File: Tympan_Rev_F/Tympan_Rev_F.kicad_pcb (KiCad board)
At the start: 4 copper layers, 38 x 74 mm, 93 parts, among them IC1 BC127, J1 SJ-3523-SMT-TR, J2 SJ-3524-SMT-TR-PI, J3 Conn_01x06, J4 Qwiik Connector, J5 Conn_01x24, J6 Conn_01x24, P1 CONN_01X06, P2 CONN_01X06, P3 CONN_01X06, P4 CONN_01X06, P6 CONN_01X01, P7 CONN_01X01, P8 CONN_01X01, SW1 CL-SB-22A, SW2 SW_Push, U1 MCP73831, U2 TLV320AIC3206IRSBT, U3 74LVC1G66, U4 LP5907MFX-1.8, U5 Teensy4.1, U6 LC709203

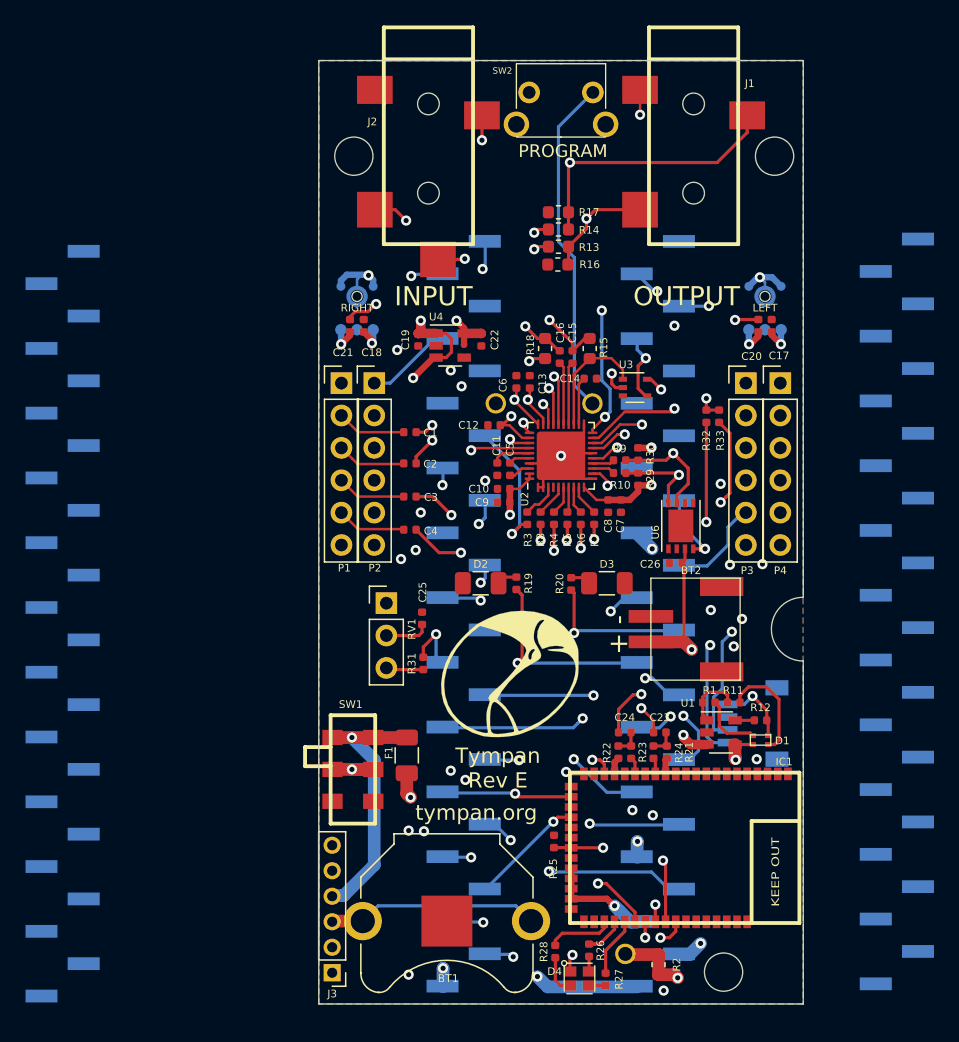
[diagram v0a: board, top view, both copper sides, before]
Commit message: Added SPI
Selected pins to bring SPI connection to the BLE moudule
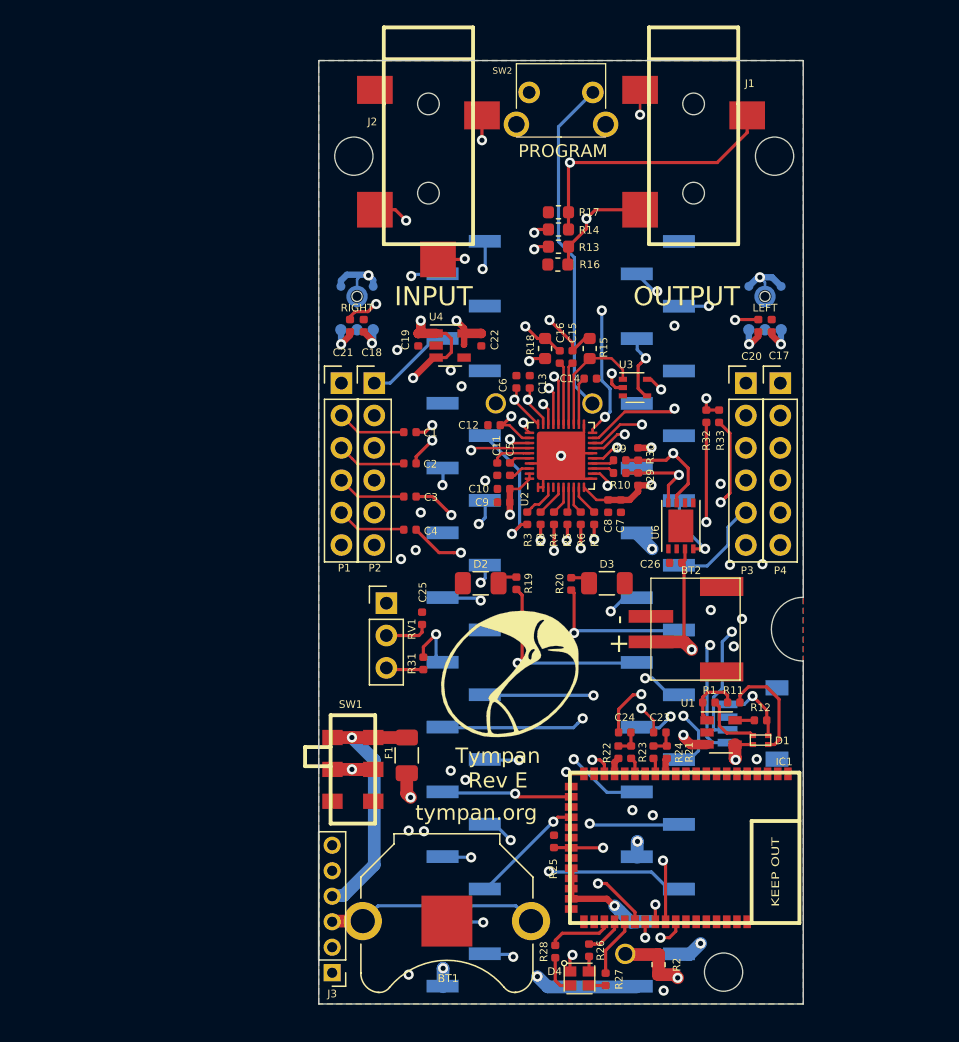
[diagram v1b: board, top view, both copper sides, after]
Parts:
- removed J5, J6: Conn_01x24, Pin_Headers:Pin_Header_Straight_1x24_Pitch2.54mm_SMD_Pin1Left

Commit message: minor edit save
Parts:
- moved J3 0.07 mm to (135.4, 130.7)
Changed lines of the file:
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@@
   )
   (footprint "Pin_Headers:Pin_Header_Straight_1x06_Pitch2.00mm" (layer "F.Cu")
-    (at 135.45 130.75 180)
+    (at 135.4 130.7 180)
     (descr "Through hole straight pin header, 1x06, 2.00mm pitch, single row")
     (tags "Through hole pin header THT 1x06 2.00mm single row")
@@
   (segment (start 142.65 128.1) (end 142.65 119.65) (width 0.25) (layer "In2.Cu") (net 135))
   (segment (start 164.375001 105.051999) (end 164.375001 114.624999) (width 0.25) (layer "In2.Cu") (net 135))
-  (segment (start 135.45 130.75) (end 140 130.75) (width 0.25) (layer "In2.Cu") (net 135))
+  (segment (start 135.4 130.7) (end 139.95 130.7) (width 0.25) (layer "In2.Cu") (net 135))
   (segment (start 162.65 78.47) (end 164.98 78.47) (width 0.25) (layer "B.Cu") (net 135))
   (segment (start 164.98 78.47) (end 165 78.45) (width 0.25) (layer "B.Cu") (net 135))

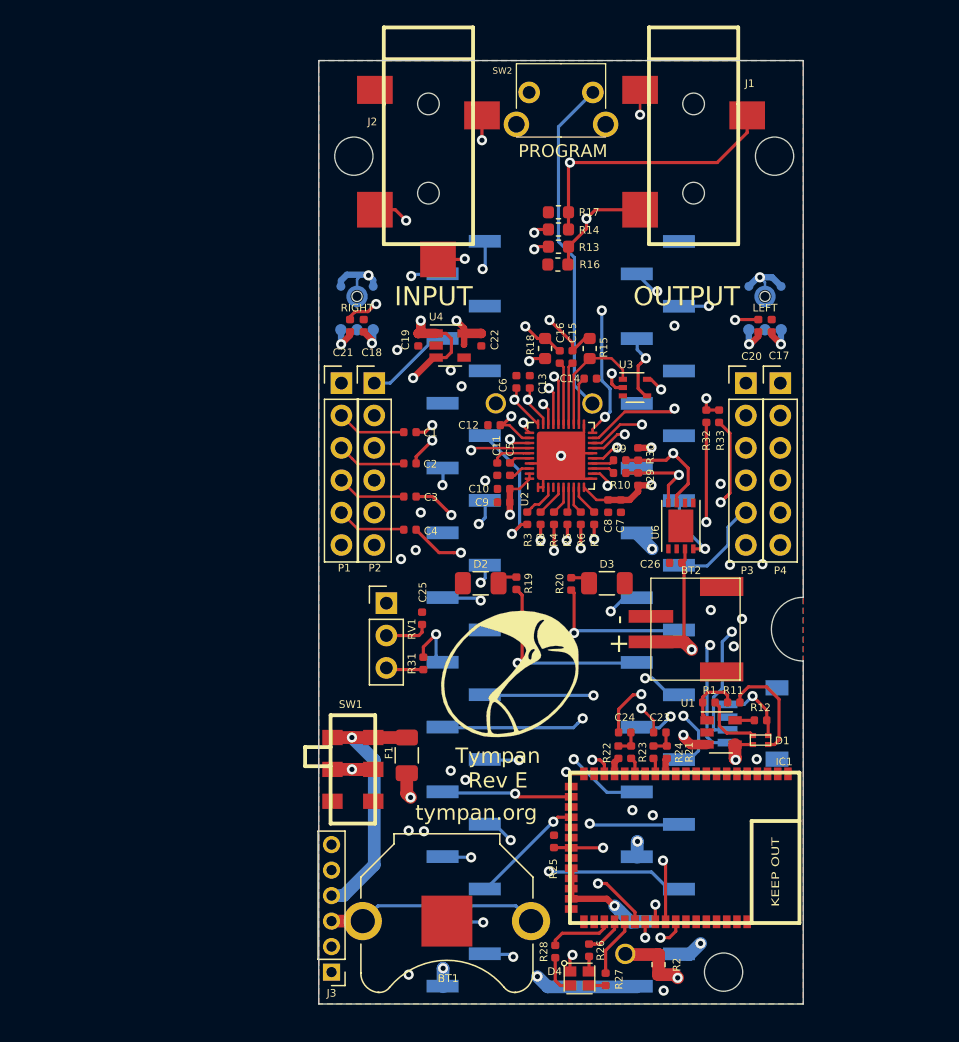
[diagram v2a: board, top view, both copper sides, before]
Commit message: First pass at routing
Have all circuits routed exept for nRF52 program header. Got to figure out the footprint and placement.
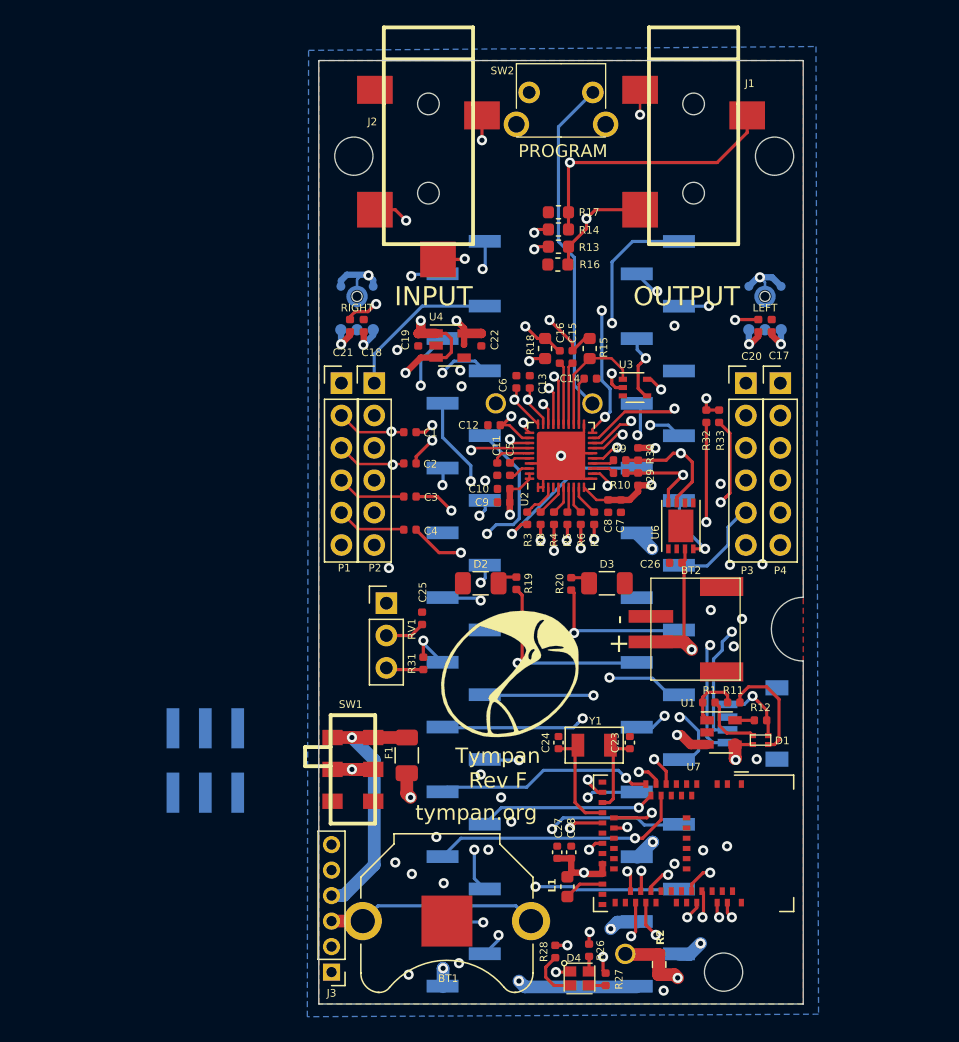
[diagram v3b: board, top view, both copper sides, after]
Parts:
- removed IC1: BC127, Tympan:BC127
- removed R21, R22: 1K, Resistor_SMD:R_0402_1005Metric
- removed R23, R24: 10K, Resistor_SMD:R_0402_1005Metric
- removed R25: 100K, Resistor_SMD:R_0402_1005Metric
- added C27: 10uF, Capacitor_SMD:C_0402_1005Metric, F.Cu at (153.1, 121.3)
- added C28: 0.1uF, Capacitor_SMD:C_0402_1005Metric, F.Cu at (154.2, 121.3)
- added J7: J-Link, Connector_PinHeader_2.54mm:PinHeader_2x03_P2.54mm_Vertical_SMD, B.Cu at (125.5, 114.1)
- added L1: DNP, Capacitor_SMD:C_0603_1608Metric, F.Cu at (153.9, 124.0)
- added U7: MDBT50Q-1MV2, RF_Module:Raytac_MDBT50Q, F.Cu at (163.8, 120.6)
- added Y1: 32.768, Tympan:XTAL, F.Cu at (156.0, 112.9)
- C23, C24: value 2.2uF -> 22pF
- R26, R27, R28: value 470R -> 1K
- moved C24 5.26 mm to (153.2, 112.7), turned to 90 degrees
- moved C23 2.48 mm to (158.8, 112.7), turned to 90 degrees
- moved R2 0.05 mm to (161.1, 130.1), turned to 90 degrees
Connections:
- net +3V3 renamed +3.3V
- net /LED_A renamed /LED_G
- net /SS renamed /CS
- C23 pad 1: /IN1_L -> Net-(U7-XL1/P0.00)
- C23 pad 2: Net-(C23-Pad2) -> GND
- C24 pad 1: /IN1_R -> Net-(U7-XL2/P0.01)
- C24 pad 2: Net-(C24-Pad2) -> GND
- MIC1 pad 5: Net-(MIC1-Pad5) -> unconnected-(MIC1-OUT--Pad5)
- MIC2 pad 5: Net-(MIC2-Pad5) -> unconnected-(MIC2-OUT--Pad5)
- P6 pad : Net-(P6-Pad1) -> (no net)
- P7 pad : Net-(P7-Pad1) -> (no net)
- P8 pad : Net-(P8-Pad1) -> (no net)
- SW1 pad 3: Net-(SW1-Pad3) -> unconnected-(SW1-NO-Pad3)
- SW1 pad 6: Net-(SW1-Pad6) -> unconnected-(SW1-NO-Pad6)
- U2 pad 4: Net-(U2-Pad4) -> unconnected-(U2-GPIO/MFP5-Pad4)
- U4 pad 4: Net-(U4-Pad4) -> unconnected-(U4-NC-Pad4)
- U5 pad 18: /nRESET -> /MOSI1
- U5 pad 19: Net-(U5-Pad19) -> /SCK1
- U5 pad 2: /BT_TX -> /BT_RTS
- U5 pad 20: Net-(U5-Pad20) -> /BT_RX
- U5 pad 21: /M_BIAS_1 -> /BT_TX
- U5 pad 22: Net-(U5-Pad22) -> /M_BIAS_1
- U5 pad 25: Net-(U5-Pad25) -> /MCLK2
- U5 pad 29: Net-(U5-Pad29) -> unconnected-(U5-37_CS-Pad29)
- U5 pad 3: /BT_RX -> /BT_CTS
- U5 pad 30: Net-(U5-Pad30) -> /BT_CS
- U5 pad 31: Net-(U5-Pad31) -> /MISO1
- U5 pad 32: Net-(U5-Pad32) -> /nRESET
- U5 pad 36: /VREGEN -> unconnected-(U5-14_A0_TX3_SPDIF_OUT-Pad36)
- U5 pad 4: /BT_PIO5 -> /OUT2
- U5 pad 5: /BT_CTS -> /LRCLK2
- U5 pad 6: /BT_RTS -> /BCLK2
- U5 pad 7: /BT_PIO0 -> /IN2
- U6 pad 5: Net-(U6-Pad5) -> unconnected-(U6-T_SW-Pad5)
- U6 pad 6: Net-(U6-Pad6) -> unconnected-(U6-T_SENSE-Pad6)
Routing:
- net /SCK1: track 0.00 -> 65.4 mm, vias 0 -> 3
- net /BT_TX: track 14.7 -> 72.9 mm, vias 2 -> 4
- net /MCLK2: track 0.00 -> 49.6 mm, vias 0 -> 2
- net /MOSI1: track 0.00 -> 48.8 mm, vias 0 -> 3
- net /MISO1: track 0.00 -> 48.0 mm, vias 0 -> 2
- net /BT_RX: track 20.2 -> 66.5 mm, vias 2 -> 3
- net /BT_CS: track 0.00 -> 40.4 mm, vias 0 -> 2
- net /LOL: track 57.6 -> 26.0 mm, vias 5 -> 3
- net /LOR: track 58.7 -> 27.8 mm, vias 5 -> 3
- net /IN1_R: track 50.5 -> 23.2 mm, vias 3 -> 2
- net /OUT2: track 0.00 -> 26.0 mm, vias 0 -> 3
- net /VREGEN: track 25.2 -> 0.00 mm, vias 2 -> 0
- net /IN1_L: track 46.6 -> 21.9 mm, vias 3 -> 2
- net /LRCLK2: track 0.00 -> 20.2 mm, vias 0 -> 1
- net /V_USB: track 27.3 -> 8.30 mm
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- added copper zone on In2.Cu, net /V_USB
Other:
- board text added: "Tympan Rev F"
- board text removed: "Tympan Rev E"

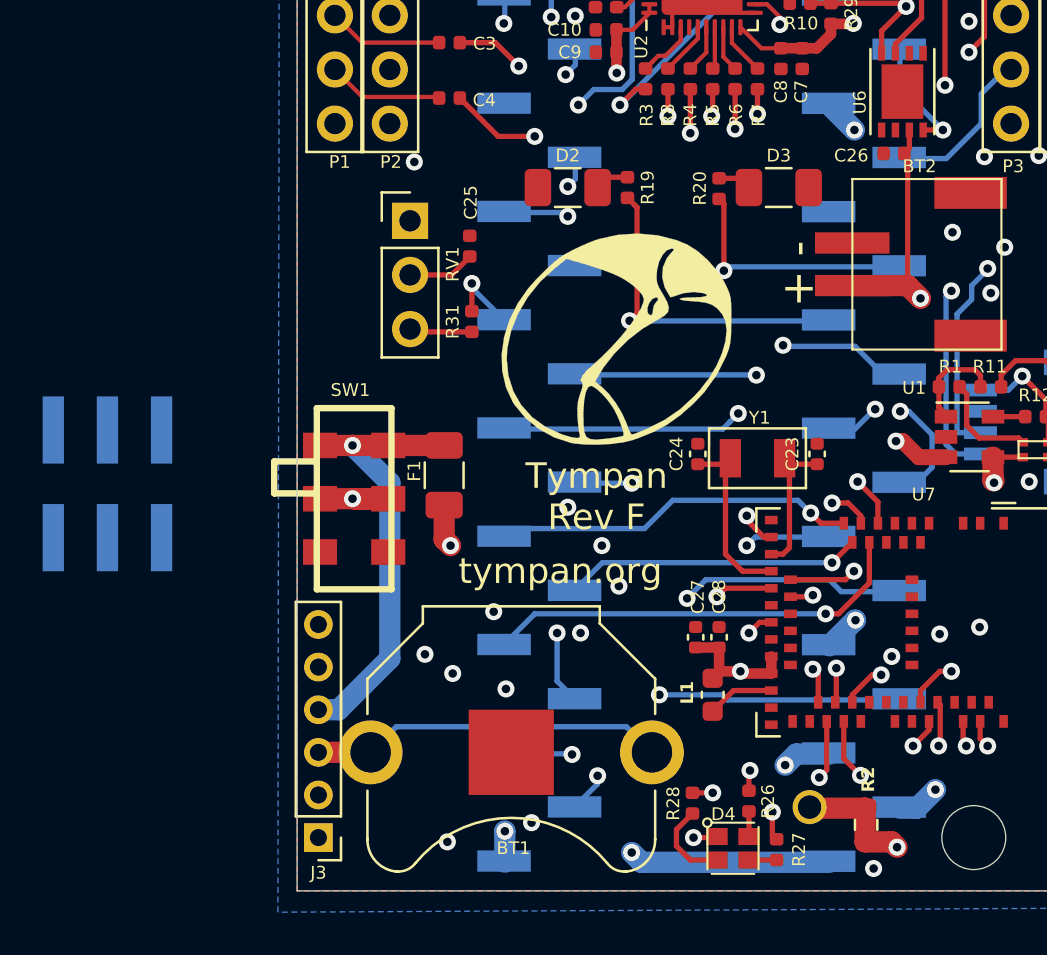
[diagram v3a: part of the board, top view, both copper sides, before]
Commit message: first pass at laying out the J-Link interface
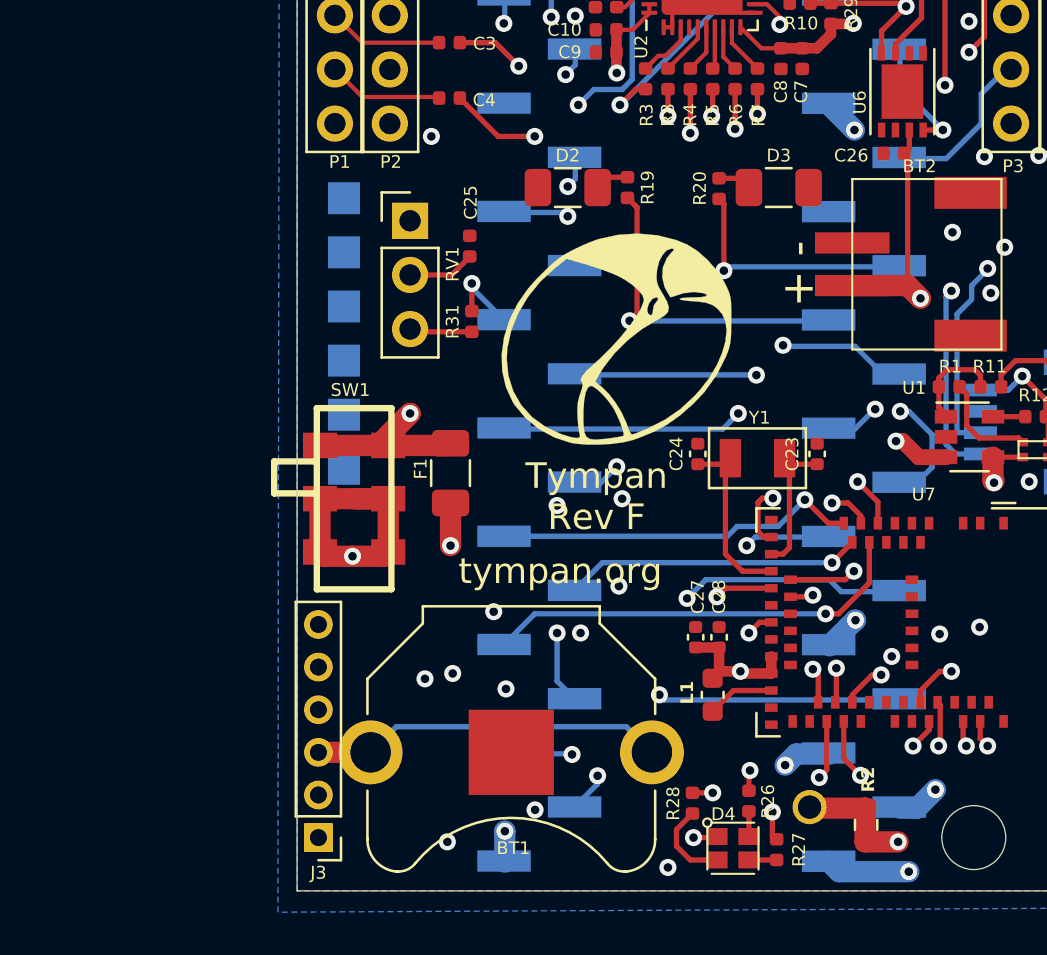
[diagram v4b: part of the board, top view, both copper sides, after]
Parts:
- J7: footprint Connector_PinHeader_2.54mm:PinHeader_2x03_P2.54mm_Vertical_SMD -> Solutions:J-Link_SMT_SIP_0.1inP
- moved J7 13.1 mm to (136.6, 107.0), turned to 90 degrees
- moved F1 0.32 mm to (141.6, 113.6)
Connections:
- J7 pad 4: /BT_nRESET -> +3.3V
- J7 pad 5: +3.3V -> /BT_nRESET
- SW1 pad 3: unconnected-(SW1-NO-Pad3) -> +BATT
- SW1 pad 6: unconnected-(SW1-NO-Pad6) -> +BATT
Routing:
- net /VIN: track 54.2 -> 48.6 mm
- net /SW_BATT: track 20.7 -> 25.8 mm
- net +BATT: track 55.7 -> 60.5 mm
- net /BT_nRESET: track 64.3 -> 60.5 mm
- net /BT_CTS: track 22.7 -> 26.2 mm
- net /WCLK: track 49.3 -> 47.9 mm
- net /34_RX8: track 83.2 -> 82.5 mm
- net /BT_RX: track 66.5 -> 67.0 mm
